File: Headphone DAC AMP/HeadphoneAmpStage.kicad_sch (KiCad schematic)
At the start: 36 parts, among them U12 OPA1612AxD, U13 OPA1612AxD, U3 TPA6120A2DWP, U4 OPA1612AxD, U5 OPA1612AxD

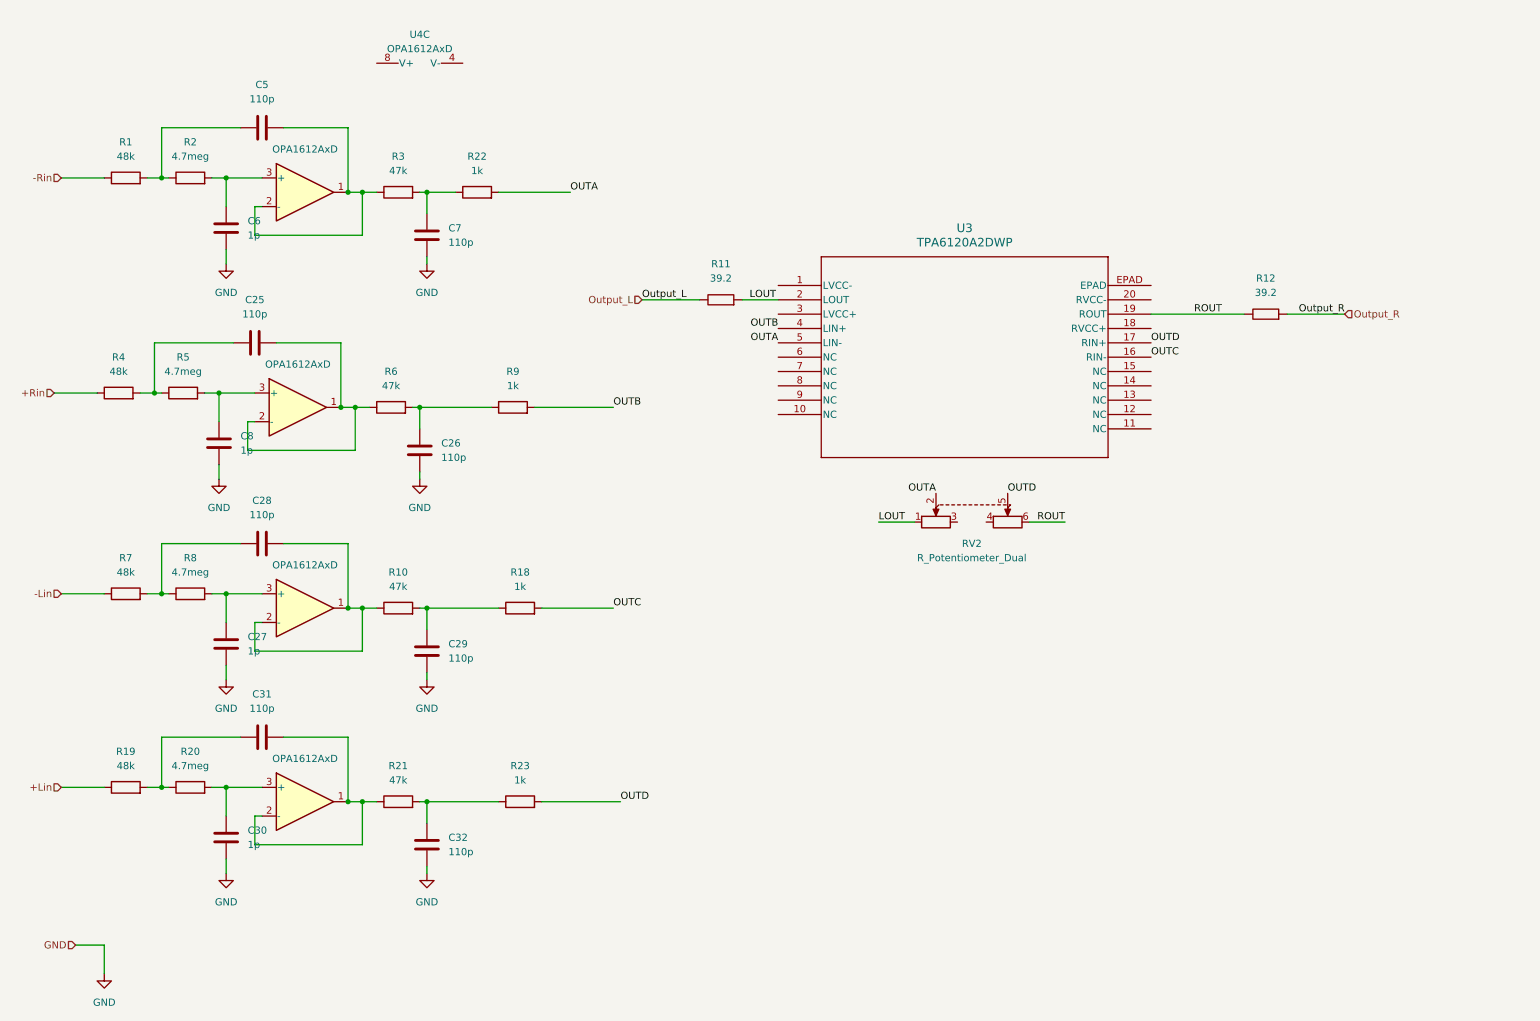
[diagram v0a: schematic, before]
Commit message: Polished DAC GPIOs and connected to XMOS
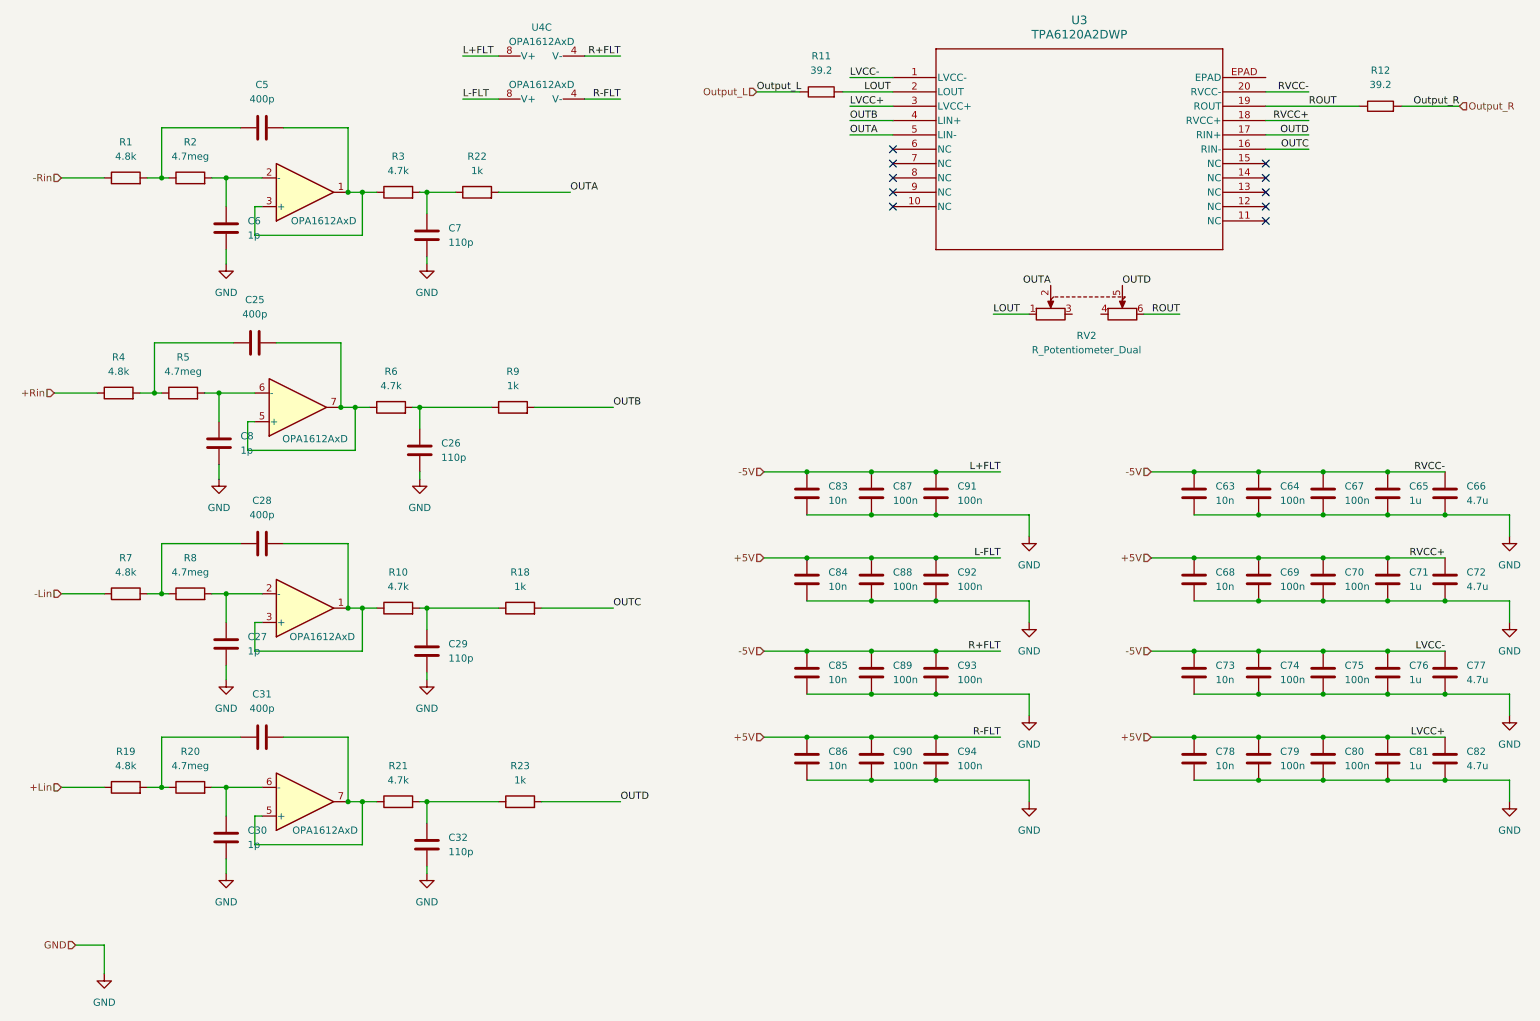
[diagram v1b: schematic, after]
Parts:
- removed U12, U13: OPA1612AxD, symbol Amplifier_Operational:OPA1612AxD
- added C63, C68, C73, C78, C83, C84, C85, C86: 10n, symbol Device:C
- added C64, C67, C69, C70, C74, C75, C79, C80, C87, C88, C89, C90, C91, C92, C93, C94: 100n, symbol Device:C
- added C65, C71, C76, C81: 1u, symbol Device:C
- added C66, C72, C77, C82: 4.7u, Capacitor_SMD:C_0805_2012Metric_Pad1.18x1.45mm_HandSolder, symbol Device:C
- C25, C28, C31, C5: value 110p -> 400p
- R1, R19, R4, R7: value 48k -> 4.8k
- R10, R21, R3, R6: value 47k -> 4.7k
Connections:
- net GND: now also C63.2, C64.2, C65.2, C66.2, C67.2, C68.2, C69.2, C70.2, C71.2, C72.2, C73.2, C74.2, C75.2, C76.2, C77.2, C78.2, C79.2, C80.2, C81.2, C82.2, C83.2, C84.2, C85.2, C86.2, C87.2, C88.2, C89.2, C90.2, C91.2, C92.2, C93.2, C94.2
- net at C30.1, R20.2: now also U5.6 (-)
- net at C27.1, R8.2: now also U5.2 (-)
- net at C8.1, R5.2: now also U4.6 (-); no longer U5.3 (+)
- net at C6.1, R2.2: now also U4.2 (-); no longer U4.3 (+)
- net at C5.2, R3.1, U4.1: now also U4.3 (+); no longer U4.2 (-)
- net at C25.2, R6.1: now also U4.5 (+), U4.7; no longer U5.1, U5.2 (-)
- net at C28.2, R10.1: now also U5.1, U5.3 (+)
- net at C31.2, R21.1: now also U5.5 (+), U5.7
- net -5V: now reaches U4.4 (V-)
- net -5V: now also U3.1 (LVCC-), U3.20 (RVCC-), U4.8 (V+), C63.1, C64.1, C65.1, C66.1, C67.1, C73.1, C74.1, C75.1, C76.1, C77.1, C83.1, C85.1, C87.1, C89.1, C91.1, C93.1
- net +5V: now reaches U3.18 (RVCC+)
- net +5V: now also U3.3 (LVCC+), U5.4 (V-), U5.8 (V+), C68.1, C69.1, C70.1, C71.1, C72.1, C78.1, C79.1, C80.1, C81.1, C82.1, C84.1, C86.1, C88.1, C90.1, C92.1, C94.1
- no-connect marks 0 -> 10
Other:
- moved on the sheet: R11, R12, RV2, U3, U4C

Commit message: "fuck my chud life"
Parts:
- added unit 2 of U4
- added unit 2 of U5
- added unit 1 of U5
- C63, C64, C65, C67, C68, C69, C70, C71, C73, C74, C75, C76, C78, C79, C80, C81, C83, C84, C85, C86, C87, C88, C89, C90, C91, C92, C93, C94: footprint (none) -> Capacitor_SMD:C_0805_2012Metric_Pad1.18x1.45mm_HandSolder
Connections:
- net at C30.1, R20.2: now also U5.6 (-); no longer U5.6 (-)
- net at C27.1, R8.2: now also U5.2 (-); no longer U5.2 (-)
- net at C8.1, R5.2: now also U4.6 (-); no longer U4.6 (-)
- net at C25.2, R6.1: now also U4.5 (+), U4.7; no longer U4.5 (+), U4.7
- net at C28.2, R10.1: now also U5.1, U5.3 (+); no longer U5.1, U5.3 (+)
- net at C31.2, R21.1: now also U5.5 (+), U5.7; no longer U5.5 (+), U5.7
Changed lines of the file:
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@@
 			)
 		)
-		(property "Footprint" ""
+		(property "Footprint" "Capacitor_SMD:C_0805_2012Metric_Pad1.18x1.45mm_HandSolder"
 			(at 258.7752 151.13 0)
 			(effects
@@
 			)
 		)
-		(property "Footprint" ""
+		(property "Footprint" "Capacitor_SMD:C_0805_2012Metric_Pad1.18x1.45mm_HandSolder"
 			(at 167.3352 135.89 0)
 			(effects
@@
 			)
 		)
-		(property "Footprint" ""
+		(property "Footprint" "Capacitor_SMD:C_0805_2012Metric_Pad1.18x1.45mm_HandSolder"
 			(at 224.4852 135.89 0)
 			(effects
@@
 			)
 		)
-		(property "Footprint" ""
+		(property "Footprint" "Capacitor_SMD:C_0805_2012Metric_Pad1.18x1.45mm_HandSolder"
 			(at 247.3452 119.38 0)
 			(effects
@@
 			)
 		)
-		(property "Footprint" ""
+		(property "Footprint" "Capacitor_SMD:C_0805_2012Metric_Pad1.18x1.45mm_HandSolder"
 			(at 178.7652 104.14 0)
 			(effects
@@
 			)
 		)
-		(property "Footprint" ""
+		(property "Footprint" "Capacitor_SMD:C_0805_2012Metric_Pad1.18x1.45mm_HandSolder"
 			(at 247.3452 151.13 0)
 			(effects
@@
 			)
 		)
-		(property "Footprint" ""
+		(property "Footprint" "Capacitor_SMD:C_0805_2012Metric_Pad1.18x1.45mm_HandSolder"
 			(at 178.7652 151.13 0)
 			(effects
@@
 			)
 		)
-		(property "Footprint" ""
+		(property "Footprint" "Capacitor_SMD:C_0805_2012Metric_Pad1.18x1.45mm_HandSolder"
 			(at 178.7652 119.38 0)
 			(effects
@@
 			)
 		)
-		(property "Footprint" ""
+		(property "Footprint" "Capacitor_SMD:C_0805_2012Metric_Pad1.18x1.45mm_HandSolder"
 			(at 155.9052 151.13 0)
 			(effects
@@
 			)
 		)
-		(property "Footprint" ""
+		(property "Footprint" "Capacitor_SMD:C_0805_2012Metric_Pad1.18x1.45mm_HandSolder"
 			(at 224.4852 119.38 0)
 			(effects
@@
 			)
 		)
-		(property "Footprint" ""
+		(property "Footprint" "Capacitor_SMD:C_0805_2012Metric_Pad1.18x1.45mm_HandSolder"
 			(at 167.3352 119.38 0)
 			(effects
@@
 			)
 		)
-		(property "Footprint" ""
+		(property "Footprint" "Capacitor_SMD:C_0805_2012Metric_Pad1.18x1.45mm_HandSolder"
 			(at 235.9152 119.38 0)
 			(effects
@@
 			)
 		)
-		(property "Footprint" ""
+		(property "Footprint" "Capacitor_SMD:C_0805_2012Metric_Pad1.18x1.45mm_HandSolder"
 			(at 224.4852 104.14 0)
 			(effects
@@
 			)
 		)
-		(property "Footprint" ""
+		(property "Footprint" "Capacitor_SMD:C_0805_2012Metric_Pad1.18x1.45mm_HandSolder"
 			(at 247.3452 104.14 0)
 			(effects
@@
 			)
 		)
-		(property "Footprint" ""
+		(property "Footprint" "Capacitor_SMD:C_0805_2012Metric_Pad1.18x1.45mm_HandSolder"
 			(at 235.9152 135.89 0)
 			(effects
@@
 			)
 		)
-		(property "Footprint" ""
+		(property "Footprint" "Capacitor_SMD:C_0805_2012Metric_Pad1.18x1.45mm_HandSolder"
 			(at 178.7652 135.89 0)
 			(effects
@@
 			)
 		)
-		(property "Footprint" ""
+		(property "Footprint" "Capacitor_SMD:C_0805_2012Metric_Pad1.18x1.45mm_HandSolder"
 			(at 224.4852 151.13 0)
 			(effects
@@
 			)
 		)
-		(property "Footprint" ""
+		(property "Footprint" "Capacitor_SMD:C_0805_2012Metric_Pad1.18x1.45mm_HandSolder"
 			(at 258.7752 119.38 0)
 			(effects
@@
 			)
 		)
-		(property "Footprint" ""
+		(property "Footprint" "Capacitor_SMD:C_0805_2012Metric_Pad1.18x1.45mm_HandSolder"
 			(at 167.3352 151.13 0)
 			(effects
@@
 			)
 		)
-		(property "Footprint" ""
+		(property "Footprint" "Capacitor_SMD:C_0805_2012Metric_Pad1.18x1.45mm_HandSolder"
 			(at 155.9052 104.14 0)
 			(effects
@@
 			)
 		)
-		(property "Footprint" ""
+		(property "Footprint" "Capacitor_SMD:C_0805_2012Metric_Pad1.18x1.45mm_HandSolder"
 			(at 235.9152 104.14 0)
 			(effects
@@
 			)
 		)
-		(property "Footprint" ""
+		(property "Footprint" "Capacitor_SMD:C_0805_2012Metric_Pad1.18x1.45mm_HandSolder"
 			(at 258.7752 135.89 0)
 			(effects
@@
 			)
 		)
-		(property "Footprint" ""
+		(property "Footprint" "Capacitor_SMD:C_0805_2012Metric_Pad1.18x1.45mm_HandSolder"
 			(at 235.9152 151.13 0)
 			(effects
@@
 			)
 		)
-		(property "Footprint" ""
+		(property "Footprint" "Capacitor_SMD:C_0805_2012Metric_Pad1.18x1.45mm_HandSolder"
 			(at 167.3352 104.14 0)
 			(effects
@@
 			)
 		)
-		(property "Footprint" ""
+		(property "Footprint" "Capacitor_SMD:C_0805_2012Metric_Pad1.18x1.45mm_HandSolder"
 			(at 258.7752 104.14 0)
 			(effects
@@
 			)
 		)
-		(property "Footprint" ""
+		(property "Footprint" "Capacitor_SMD:C_0805_2012Metric_Pad1.18x1.45mm_HandSolder"
 			(at 155.9052 135.89 0)
 			(effects
@@
 			)
 		)
-		(property "Footprint" ""
+		(property "Footprint" "Capacitor_SMD:C_0805_2012Metric_Pad1.18x1.45mm_HandSolder"
 			(at 155.9052 119.38 0)
 			(effects
@@
 			)
 		)
-		(property "Footprint" ""
+		(property "Footprint" "Capacitor_SMD:C_0805_2012Metric_Pad1.18x1.45mm_HandSolder"
 			(at 247.3452 135.89 0)
 			(effects

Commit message: uPDATED fOOTPRINTS
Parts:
- U4, U5: footprint (none) -> Package_SO:SOIC-8-1EP_3.9x4.9mm_P1.27mm_EP2.95x4.9mm_Mask2.71x3.4mm_ThermalVias
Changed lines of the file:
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@@
 			)
 		)
-		(property "Footprint" ""
+		(property "Footprint" "Package_SO:SOIC-8-1EP_3.9x4.9mm_P1.27mm_EP2.95x4.9mm_Mask2.71x3.4mm_ThermalVias"
 			(at 66.04 46.99 0)
 			(effects
@@
 			)
 		)
-		(property "Footprint" ""
+		(property "Footprint" "Package_SO:SOIC-8-1EP_3.9x4.9mm_P1.27mm_EP2.95x4.9mm_Mask2.71x3.4mm_ThermalVias"
 			(at 64.77 85.09 0)
 			(effects
@@
 			)
 		)
-		(property "Footprint" ""
+		(property "Footprint" "Package_SO:SOIC-8-1EP_3.9x4.9mm_P1.27mm_EP2.95x4.9mm_Mask2.71x3.4mm_ThermalVias"
 			(at 107.95 27.94 0)
 			(effects
@@
 			)
 		)
-		(property "Footprint" ""
+		(property "Footprint" "Package_SO:SOIC-8-1EP_3.9x4.9mm_P1.27mm_EP2.95x4.9mm_Mask2.71x3.4mm_ThermalVias"
 			(at 66.04 154.94 0)
 			(effects
@@
 			)
 		)
-		(property "Footprint" ""
+		(property "Footprint" "Package_SO:SOIC-8-1EP_3.9x4.9mm_P1.27mm_EP2.95x4.9mm_Mask2.71x3.4mm_ThermalVias"
 			(at 66.04 120.65 0)
 			(effects
@@
 			)
 		)
-		(property "Footprint" ""
+		(property "Footprint" "Package_SO:SOIC-8-1EP_3.9x4.9mm_P1.27mm_EP2.95x4.9mm_Mask2.71x3.4mm_ThermalVias"
 			(at 107.95 20.32 0)
 			(effects

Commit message: uPDATED MORE FOOTPRINTS
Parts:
- C63, C64, C67, C68, C69, C70, C73, C74, C75, C78, C79, C80, C83, C84, C85, C86, C87, C88, C89, C90, C91, C92, C93, C94: footprint Capacitor_SMD:C_0805_2012Metric_Pad1.18x1.45mm_HandSolder -> Capacitor_SMD:C_0402_1005Metric_Pad0.74x0.62mm_HandSolder
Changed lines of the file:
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@@
 			)
 		)
-		(property "Footprint" "Capacitor_SMD:C_0805_2012Metric_Pad1.18x1.45mm_HandSolder"
+		(property "Footprint" "Capacitor_SMD:C_0402_1005Metric_Pad0.74x0.62mm_HandSolder"
 			(at 167.3352 135.89 0)
 			(effects
@@
 			)
 		)
-		(property "Footprint" "Capacitor_SMD:C_0805_2012Metric_Pad1.18x1.45mm_HandSolder"
+		(property "Footprint" "Capacitor_SMD:C_0402_1005Metric_Pad0.74x0.62mm_HandSolder"
 			(at 224.4852 135.89 0)
 			(effects
@@
 			)
 		)
-		(property "Footprint" "Capacitor_SMD:C_0805_2012Metric_Pad1.18x1.45mm_HandSolder"
+		(property "Footprint" "Capacitor_SMD:C_0402_1005Metric_Pad0.74x0.62mm_HandSolder"
 			(at 247.3452 119.38 0)
 			(effects
@@
 			)
 		)
-		(property "Footprint" "Capacitor_SMD:C_0805_2012Metric_Pad1.18x1.45mm_HandSolder"
+		(property "Footprint" "Capacitor_SMD:C_0402_1005Metric_Pad0.74x0.62mm_HandSolder"
 			(at 178.7652 104.14 0)
 			(effects
@@
 			)
 		)
-		(property "Footprint" "Capacitor_SMD:C_0805_2012Metric_Pad1.18x1.45mm_HandSolder"
+		(property "Footprint" "Capacitor_SMD:C_0402_1005Metric_Pad0.74x0.62mm_HandSolder"
 			(at 247.3452 151.13 0)
 			(effects
@@
 			)
 		)
-		(property "Footprint" "Capacitor_SMD:C_0805_2012Metric_Pad1.18x1.45mm_HandSolder"
+		(property "Footprint" "Capacitor_SMD:C_0402_1005Metric_Pad0.74x0.62mm_HandSolder"
 			(at 178.7652 151.13 0)
 			(effects
@@
 			)
 		)
-		(property "Footprint" "Capacitor_SMD:C_0805_2012Metric_Pad1.18x1.45mm_HandSolder"
+		(property "Footprint" "Capacitor_SMD:C_0402_1005Metric_Pad0.74x0.62mm_HandSolder"
 			(at 178.7652 119.38 0)
 			(effects
@@
 			)
 		)
-		(property "Footprint" "Capacitor_SMD:C_0805_2012Metric_Pad1.18x1.45mm_HandSolder"
+		(property "Footprint" "Capacitor_SMD:C_0402_1005Metric_Pad0.74x0.62mm_HandSolder"
 			(at 155.9052 151.13 0)
 			(effects
@@
 			)
 		)
-		(property "Footprint" "Capacitor_SMD:C_0805_2012Metric_Pad1.18x1.45mm_HandSolder"
+		(property "Footprint" "Capacitor_SMD:C_0402_1005Metric_Pad0.74x0.62mm_HandSolder"
 			(at 224.4852 119.38 0)
 			(effects
@@
 			)
 		)
-		(property "Footprint" "Capacitor_SMD:C_0805_2012Metric_Pad1.18x1.45mm_HandSolder"
+		(property "Footprint" "Capacitor_SMD:C_0402_1005Metric_Pad0.74x0.62mm_HandSolder"
 			(at 167.3352 119.38 0)
 			(effects
@@
 			)
 		)
-		(property "Footprint" "Capacitor_SMD:C_0805_2012Metric_Pad1.18x1.45mm_HandSolder"
+		(property "Footprint" "Capacitor_SMD:C_0402_1005Metric_Pad0.74x0.62mm_HandSolder"
 			(at 235.9152 119.38 0)
 			(effects
@@
 			)
 		)
-		(property "Footprint" "Capacitor_SMD:C_0805_2012Metric_Pad1.18x1.45mm_HandSolder"
+		(property "Footprint" "Capacitor_SMD:C_0402_1005Metric_Pad0.74x0.62mm_HandSolder"
 			(at 224.4852 104.14 0)
 			(effects
@@
 			)
 		)
-		(property "Footprint" "Capacitor_SMD:C_0805_2012Metric_Pad1.18x1.45mm_HandSolder"
+		(property "Footprint" "Capacitor_SMD:C_0402_1005Metric_Pad0.74x0.62mm_HandSolder"
 			(at 247.3452 104.14 0)
 			(effects
@@
 			)
 		)
-		(property "Footprint" "Capacitor_SMD:C_0805_2012Metric_Pad1.18x1.45mm_HandSolder"
+		(property "Footprint" "Capacitor_SMD:C_0402_1005Metric_Pad0.74x0.62mm_HandSolder"
 			(at 235.9152 135.89 0)
 			(effects
@@
 			)
 		)
-		(property "Footprint" "Capacitor_SMD:C_0805_2012Metric_Pad1.18x1.45mm_HandSolder"
+		(property "Footprint" "Capacitor_SMD:C_0402_1005Metric_Pad0.74x0.62mm_HandSolder"
 			(at 178.7652 135.89 0)
 			(effects
@@
 			)
 		)
-		(property "Footprint" "Capacitor_SMD:C_0805_2012Metric_Pad1.18x1.45mm_HandSolder"
+		(property "Footprint" "Capacitor_SMD:C_0402_1005Metric_Pad0.74x0.62mm_HandSolder"
 			(at 224.4852 151.13 0)
 			(effects
@@
 			)
 		)
-		(property "Footprint" "Capacitor_SMD:C_0805_2012Metric_Pad1.18x1.45mm_HandSolder"
+		(property "Footprint" "Capacitor_SMD:C_0402_1005Metric_Pad0.74x0.62mm_HandSolder"
 			(at 167.3352 151.13 0)
 			(effects
@@
 			)
 		)
-		(property "Footprint" "Capacitor_SMD:C_0805_2012Metric_Pad1.18x1.45mm_HandSolder"
+		(property "Footprint" "Capacitor_SMD:C_0402_1005Metric_Pad0.74x0.62mm_HandSolder"
 			(at 155.9052 104.14 0)
 			(effects
@@
 			)
 		)
-		(property "Footprint" "Capacitor_SMD:C_0805_2012Metric_Pad1.18x1.45mm_HandSolder"
+		(property "Footprint" "Capacitor_SMD:C_0402_1005Metric_Pad0.74x0.62mm_HandSolder"
 			(at 235.9152 104.14 0)
 			(effects
@@
 			)
 		)
-		(property "Footprint" "Capacitor_SMD:C_0805_2012Metric_Pad1.18x1.45mm_HandSolder"
+		(property "Footprint" "Capacitor_SMD:C_0402_1005Metric_Pad0.74x0.62mm_HandSolder"
 			(at 235.9152 151.13 0)
 			(effects
@@
 			)
 		)
-		(property "Footprint" "Capacitor_SMD:C_0805_2012Metric_Pad1.18x1.45mm_HandSolder"
+		(property "Footprint" "Capacitor_SMD:C_0402_1005Metric_Pad0.74x0.62mm_HandSolder"
 			(at 167.3352 104.14 0)
 			(effects
@@
 			)
 		)
-		(property "Footprint" "Capacitor_SMD:C_0805_2012Metric_Pad1.18x1.45mm_HandSolder"
+		(property "Footprint" "Capacitor_SMD:C_0402_1005Metric_Pad0.74x0.62mm_HandSolder"
 			(at 155.9052 135.89 0)
 			(effects
@@
 			)
 		)
-		(property "Footprint" "Capacitor_SMD:C_0805_2012Metric_Pad1.18x1.45mm_HandSolder"
+		(property "Footprint" "Capacitor_SMD:C_0402_1005Metric_Pad0.74x0.62mm_HandSolder"
 			(at 155.9052 119.38 0)
 			(effects
@@
 			)
 		)
-		(property "Footprint" "Capacitor_SMD:C_0805_2012Metric_Pad1.18x1.45mm_HandSolder"
+		(property "Footprint" "Capacitor_SMD:C_0402_1005Metric_Pad0.74x0.62mm_HandSolder"
 			(at 247.3452 135.89 0)
 			(effects
